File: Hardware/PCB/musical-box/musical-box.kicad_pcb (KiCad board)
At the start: 4 copper layers, 70 x 60 mm, 184 parts, among them J1 power, J201 PSU, J202 Jack-DC, J203 Li Ion 2S, J401 SPI Display, J402 Rotary Encoder 1, J403 I2C Display, J404 Rotary Encoder 2, J405 WS2812, J501 spk_out, J503 AudioJack4, P201 USB_C, P202 ICT-Point, P203 ICT-Point, P204 ICT-Point, Q201 DMP3017SFK, Q204 IRF9362, Q301 BC846BDW1, SW301 boot, SW302 reset, U201 STUSB4500QTR, U202 MP2615, U203 TPS56339, U204 TLV75733PDBV, U205 TLV75733PDBV, U206 TLV803EC30DBZR, U301 CH340C, U302 ESP32-WROVER, U401 PCF8574ATS, U501 SPH0644HM4H-1, U502 SPH0644HM4H-1, U503 TAS5754MDCA

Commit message: layoutoptimisation and review
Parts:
- R512: moved to B.Cu
- moved SW302 2.12 mm to (386.7, 174.0)
- moved SW301 2.12 mm to (391.7, 174.0), turned to 90 degrees
- moved R501 1.48 mm to (407.1, 181.2)
- moved R512 1.48 mm to (405.6, 181.2)
- moved C502 0.68 mm to (410.1, 180.7)
- moved U501 0.68 mm to (410.1, 182.0)
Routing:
- net /Microcontroller/I36: track 63.6 -> 77.0 mm
- net Net-(R512-Pad1): track 2.27 -> 8.90 mm, vias 0 -> 1
- net /Microcontroller/IO05: track 92.3 -> 98.8 mm, vias 5 -> 4
- net /Microcontroller/IO18: track 94.4 -> 98.6 mm, vias 6 -> 4
- net GND: track 128.3 -> 124.8 mm, vias 68 -> 75
- net /Microcontroller/IO23: track 68.4 -> 65.2 mm
- net Net-(J404-Pad2): track 26.4 -> 23.5 mm, vias 2 -> 1
- net /Microcontroller/~RESET: track 69.9 -> 67.3 mm, vias 6 -> 3
- net /Microcontroller/IO00: track 49.4 -> 47.1 mm
- net /Audio Output/GPIO0: track 43.6 -> 45.5 mm
- net /Microcontroller/IO21: track 119.4 -> 117.6 mm, vias 3 -> 2
- net Net-(J404-Pad1): track 26.9 -> 25.4 mm, vias 2 -> 1
- net /Audio Output/Detect: track 65.0 -> 63.7 mm
- net /Microcontroller/IO12: track 29.7 -> 28.5 mm
- net /Microcontroller/IO22: track 132.3 -> 133.3 mm, vias 4 -> 2
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
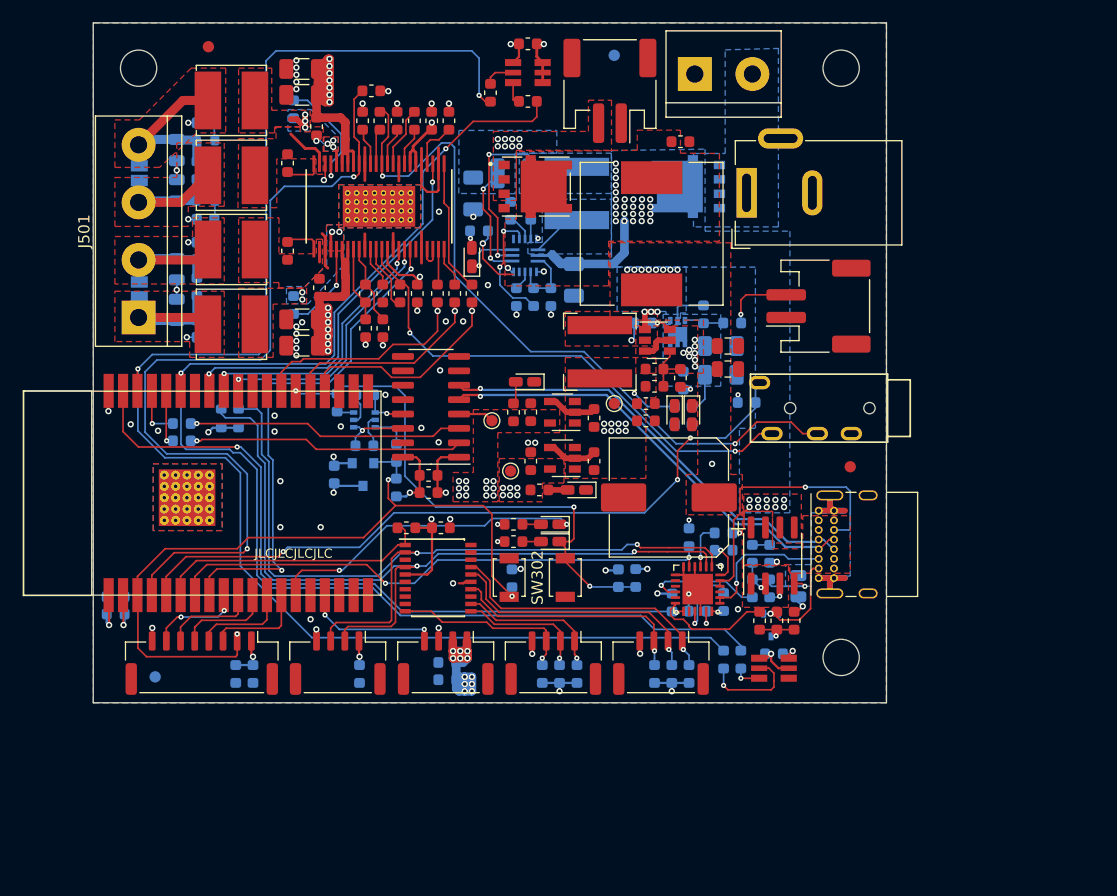
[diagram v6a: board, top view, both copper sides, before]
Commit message: Start layout rework
Added AUX-in connector and changed line in to have only a single
connector type. Due to the change, the power part has to be reworked.
First part placement is finished, layout work still ongoing.
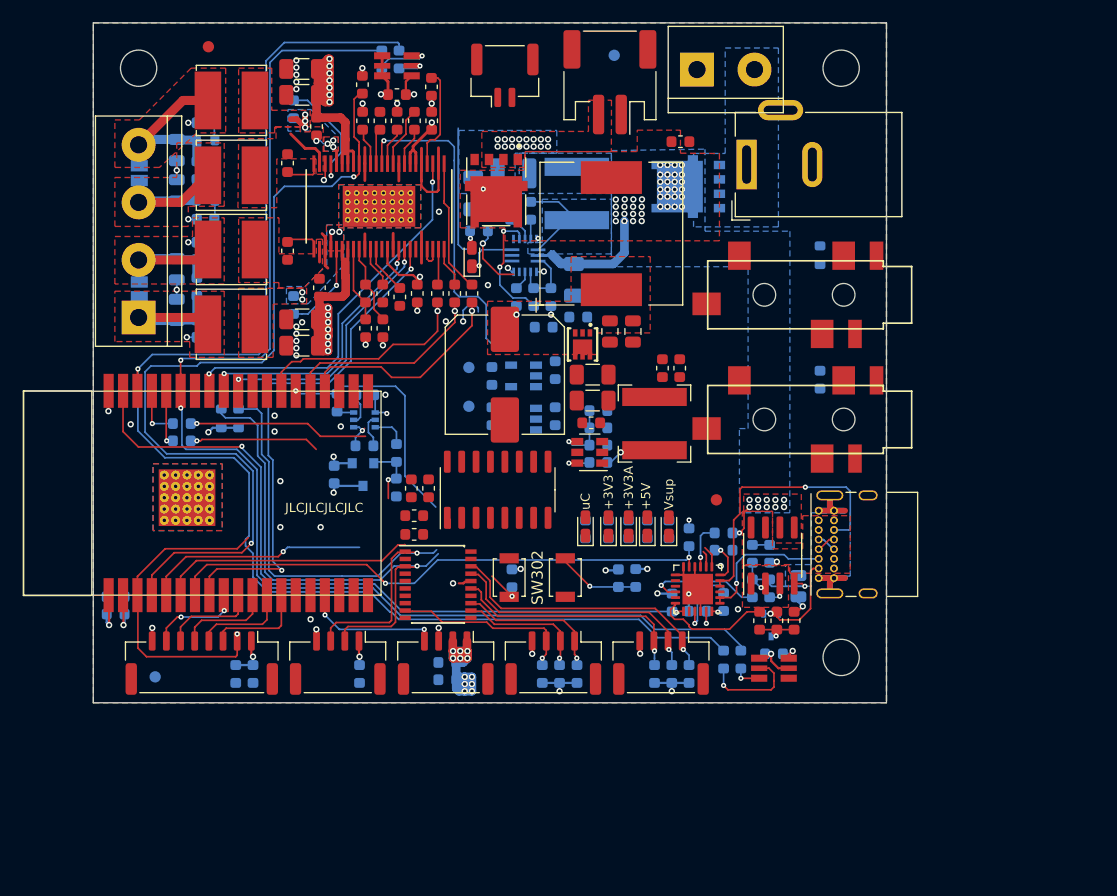
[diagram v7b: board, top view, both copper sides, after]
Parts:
- removed D101: LED, LED_SMD:LED_0603_1608Metric_Castellated
- removed P204: ICT-Point, TestPoint:TestPoint_Pad_D1.0mm
- removed R104: 1k, Resistor_SMD:R_0603_1608Metric
- added J502: aux in, SilentWorks:PJ328B, F.Cu at (419.7, 149.0)
- added R513: 10k, Resistor_SMD:R_0603_1608Metric, B.Cu at (414.1, 145.5)
- C218, C222, C224, Q201: moved to F.Cu
- C219, C221, C223, C225, C226, P202, P203, R105, R217, R219, R220, R221, R504, R505, U204, U205: moved to B.Cu
- J1: footprint Connector_JST:JST_PH_S2B-PH-SM4-TB_1x02-1MP_P2.00mm_Horizontal -> Connector_JST:JST_GH_BM02B-GHS-TBT_1x02-1MP_P1.25mm_Vertical
- J503: value AudioJack4 -> line in; footprint SilentWorks:PJ320A -> SilentWorks:PJ328B
- moved J1 34.4 mm to (386.3, 129.6), turned to 0 degrees
- moved C202 18.1 mm to (386.3, 156.0), turned to 270 degrees
- moved D207 14.7 mm to (395.5, 169.4), turned to 90 degrees
- moved R202 14.1 mm to (389.8, 151.9), turned to 180 degrees
- moved R205 13.6 mm to (392.8, 151.0)
- moved R505 13.4 mm to (375.5, 128.2), turned to 90 degrees
- moved R217 13.3 mm to (395.5, 169.7)
- moved C216 12.9 mm to (394.6, 163.8), turned to 0 degrees
- moved C501 12.4 mm to (376.8, 131.3), turned to 180 degrees
- moved C222 12.3 mm to (394.1, 158.3), turned to 0 degrees
- moved FID103 12.2 mm to (405.0, 167.1)
- moved U502 11.6 mm to (376.8, 128.8), turned to 180 degrees
- moved U203 11.6 mm to (393.8, 162.9), turned to 180 degrees
- moved C218 11.3 mm to (394.1, 156.0), turned to 0 degrees
- moved C201 10.5 mm to (395.6, 152.2), turned to 90 degrees
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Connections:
- net /Audio Output/Detect renamed /Microcontroller/I39
- C511 pad 1: /Audio Output/DAC_OUTA -> /Audio Output/SPK_INA
- C525 pad 2: /Audio Output/DAC_OUTB -> /Audio Output/SPK_INB
- J1 pad 1: GND -> Net-(J1-Pad1)
- J1 pad 2: Net-(J1-Pad2) -> GND
- J1 pad MP: (no net) -> GND
- J203 pad MP: (no net) -> GND
- R205 pad 1: Net-(J1-Pad2) -> Net-(J1-Pad1)
- U302 pad 14: /Microcontroller/IO12 -> /Audio Output/AUX_Detect
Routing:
- net /Audio Output/DAC_OUTA: track 45.6 -> 0.00 mm, vias 2 -> 0
- net /Microcontroller/I39: track 63.7 -> 19.8 mm, vias 3 -> 1
- net /Microcontroller/D-: track 39.4 -> 1.70 mm, vias 1 -> 0
- net /Microcontroller/D+: track 39.4 -> 1.70 mm, vias 1 -> 0
- net /Audio Output/DAC_OUTB: track 64.9 -> 28.3 mm, vias 2 -> 1
- net /Microcontroller/~RESET: track 67.3 -> 37.9 mm
- net /Microcontroller/IO12: track 28.5 -> 0.00 mm, vias 2 -> 0
- net +5V: track 69.5 -> 45.3 mm, vias 21 -> 12
- net /Microcontroller/IO05: track 98.8 -> 74.9 mm, vias 4 -> 3
- net /Microcontroller/IO18: track 98.6 -> 75.1 mm, vias 4 -> 3
- net +3V3: track 54.0 -> 34.5 mm, vias 28 -> 12
- net /Microcontroller/IO00: track 47.1 -> 29.0 mm, vias 3 -> 2
- net Net-(L202-Pad2): track 15.6 -> 0.00 mm, vias 2 -> 0
- net Net-(R302-Pad2): track 24.3 -> 11.5 mm
- net /Microcontroller/IO22: track 133.3 -> 123.0 mm, vias 2 -> 1
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- removed copper zone on B.Cu, net +15V
- removed copper zone on F.Cu, net +15V
- removed copper zone on F.Cu, net +3.3VA
- removed copper zone on F.Cu, net +3V3
- removed copper zone on F.Cu, net +5V
- removed copper zone on B.Cu, net Net-(C201-Pad2)
- removed copper zone on F.Cu, net Net-(C216-Pad2)
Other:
- board text added: "+3V3"
- board text added: "+3V3A"
- board text added: "+5V"
- board text added: "Vsup"
- board text added: "uC"

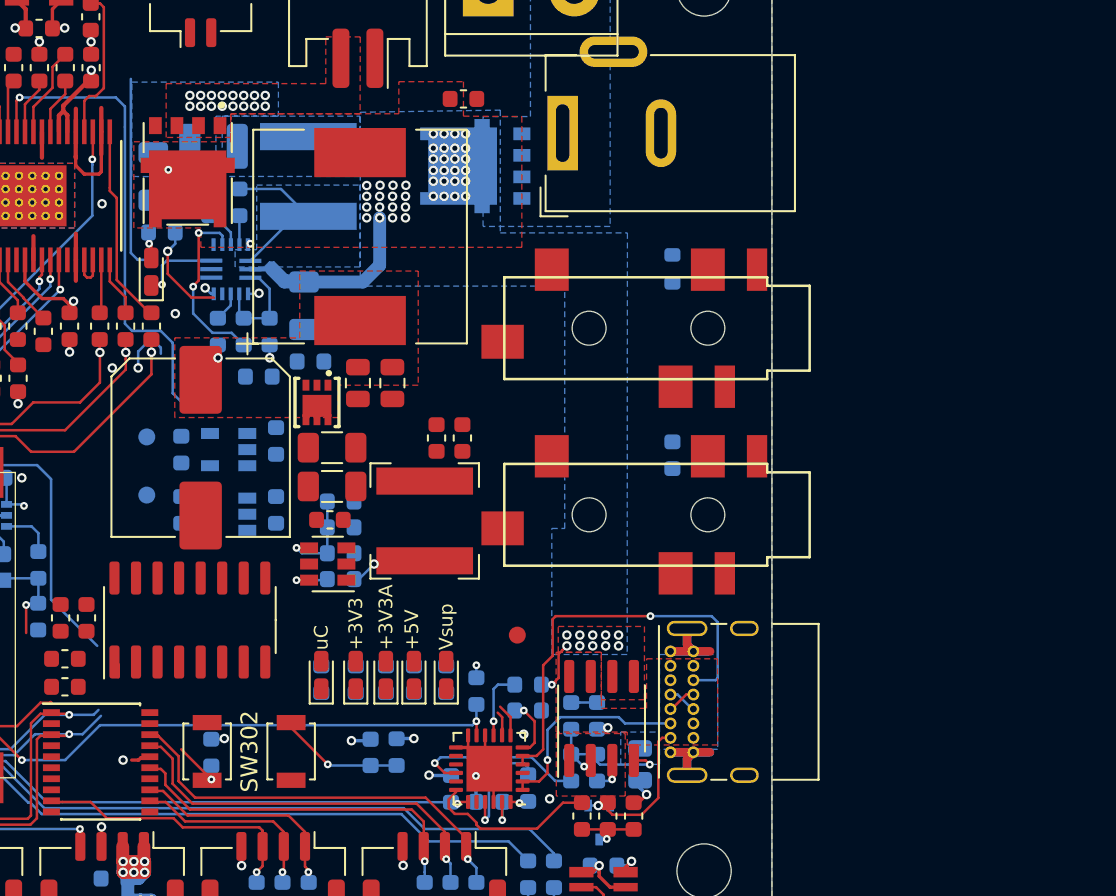
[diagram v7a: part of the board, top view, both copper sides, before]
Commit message: Change Capatictor size to 0805
Reduce the package size of the input filter capacitors
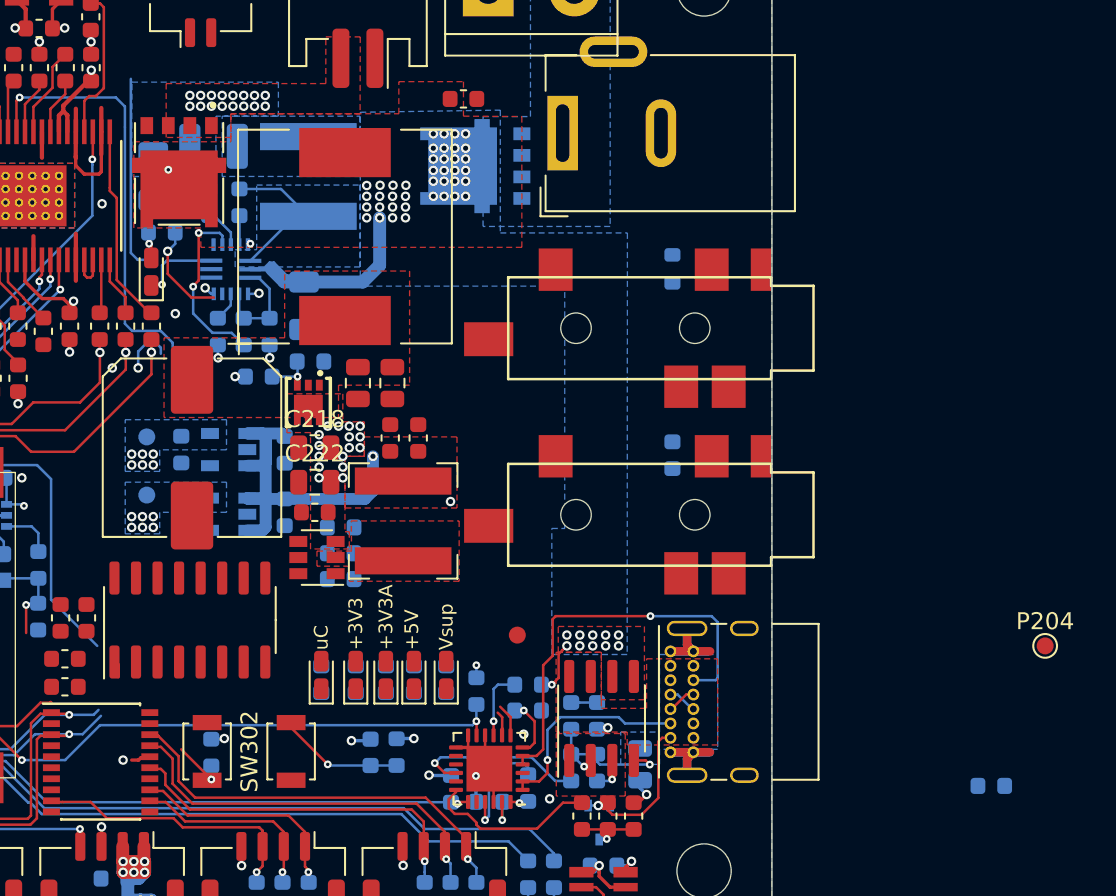
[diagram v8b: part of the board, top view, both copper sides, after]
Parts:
- added P204: ICT-Point, TestPoint:TestPoint_Pad_D1.0mm, F.Cu at (436.1, 167.7)
- C218, C222: footprint Capacitor_SMD:C_1206_3216Metric -> Capacitor_SMD:C_0805_2012Metric
- moved R219 41.9 mm to (432.9, 176.0)
- moved C217 2.73 mm to (397.5, 155.5)
- moved C220 2.60 mm to (399.1, 155.5)
- moved L203 1.27 mm to (398.3, 160.4)
- moved C222 1.05 mm to (393.1, 158.1)
- moved C218 1.02 mm to (393.1, 156.0)
- moved C224 0.99 mm to (393.1, 159.9)
- moved L201 0.89 mm to (394.8, 143.6)
- moved U203 0.74 mm to (393.2, 162.5)
- moved C223 0.73 mm to (391.3, 156.2)
- moved C225 0.53 mm to (391.3, 159.9)
- moved C202 0.51 mm to (385.8, 156.0)
- moved D204 0.51 mm to (385.1, 139.9)
- moved Q201 0.51 mm to (392.7, 153.4)
- moved J502 0.23 mm to (420.0, 149.0)
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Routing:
- net +5V: track 45.3 -> 87.6 mm, vias 12 -> 14
- net +3.3VA: track 39.2 -> 12.6 mm, vias 3 -> 9
- net Net-(C219-Pad1): track 5.74 -> 0.00 mm, vias 1 -> 0
- net Net-(Q201-Pad3): track 0.00 -> 2.91 mm, vias 0 -> 1
- net Net-(C216-Pad1): track 2.58 -> 0.00 mm, vias 1 -> 0
- net Net-(C216-Pad2): track 1.55 -> 0.00 mm, vias 1 -> 0
- net Net-(C201-Pad2): track 0.00 -> 0.61 mm, vias 0 -> 1
- net +3V3: vias 12 -> 18
- net +15V: vias 14 -> 30
- added copper zone on F.Cu, net +15V
- added copper zone on B.Cu, net +3.3VA
- added copper zone on B.Cu, net +3V3
- added copper zone on F.Cu, net +5V
- added copper zone on F.Cu, net Net-(C216-Pad2)
- removed copper zone on In1.Cu, net +3.3VA
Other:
- net class 3A: trace_width 0.8 -> 0.7
